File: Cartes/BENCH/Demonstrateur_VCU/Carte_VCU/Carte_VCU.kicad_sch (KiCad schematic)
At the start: 46 parts, among them J1 Conn_01x02_Female, J10 Conn_01x02_Female, J11 Conn_01x02_Female, J12 Conn_01x04_Female, J13 Conn_01x03_Female, J14 Conn_01x03_Female, J15 Conn_01x03_Female, J2 Conn_01x02_Female, J3 Conn_01x02_Female, J4 Conn_01x02_Female, J5 Conn_01x02_Female, J6 Conn_01x02_Female, J7 Conn_01x02_Female, J8 Conn_01x03_Female, J9 Conn_01x03_Female, SW1 SW_Push_SPDT, SW2 SW_Push_SPDT, SW3 SW_Push_SPDT, SW4 SW_Push_SPDT, SW5 SW_MEC_5G, SW6 SW_Push_SPDT, SW7 SW_Push_SPDT, SW8 SW_Push_SPDT, SW9 SW_Push_SPDT

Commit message: Ajout du dongle SCS
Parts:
- D1, D10, D11, D2, D3, D4, D5, D6, D7, D8, D9: footprint LED_THT:LED_D5.0mm -> (none)
- J1, J10, J11, J2, J3, J4, J5, J6, J7: footprint Connector_JST:JST_EH_S2B-EH_1x02_P2.50mm_Horizontal -> (none)
- J12: footprint Connector_JST:JST_EH_S4B-EH_1x04_P2.50mm_Horizontal -> (none)
- J13, J14, J15: footprint Connector_JST:JST_EH_S3B-EH_1x03_P2.50mm_Horizontal -> (none)
- J8, J9: footprint Connector_JST:JST_EH_S3B-EH_1x03_P2.50mm_Horizontal -> Connector_Wuerth:Wuerth_WR-WTB_64800311622_1x03_P1.50mm_Vertical
- SW1, SW2, SW3, SW4, SW6, SW7, SW8, SW9: footprint Connector_JST:JST_EH_B3B-EH-A_1x03_P2.50mm_Vertical -> (none)
- SW5: footprint Connector_JST:JST_EH_B2B-EH-A_1x02_P2.50mm_Vertical -> (none)

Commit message: ESF tentative
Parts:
- D1, D10, D11, D2, D3, D4, D5, D6, D7, D8, D9: footprint (none) -> LED_THT:LED_D5.0mm
- J1, J10, J11, J2, J3, J4, J5, J6, J7: footprint (none) -> Connector_JST:JST_EH_S2B-EH_1x02_P2.50mm_Horizontal
- J12: footprint (none) -> Connector_JST:JST_EH_S4B-EH_1x04_P2.50mm_Horizontal
- J13, J14, J15: footprint (none) -> Connector_JST:JST_EH_S3B-EH_1x03_P2.50mm_Horizontal
- SW1, SW2, SW3, SW4, SW6, SW7, SW8, SW9: footprint (none) -> Connector_JST:JST_EH_B3B-EH-A_1x03_P2.50mm_Vertical
- SW5: footprint (none) -> Connector_JST:JST_EH_B2B-EH-A_1x02_P2.50mm_Vertical
- renumbered R6 to R10, R7 to R11, R8 to R12, R9 to R13, R10 to R14, R11 to R15, R1 to R5, R2 to R6, R3 to R7, R4 to R8, R5 to R9

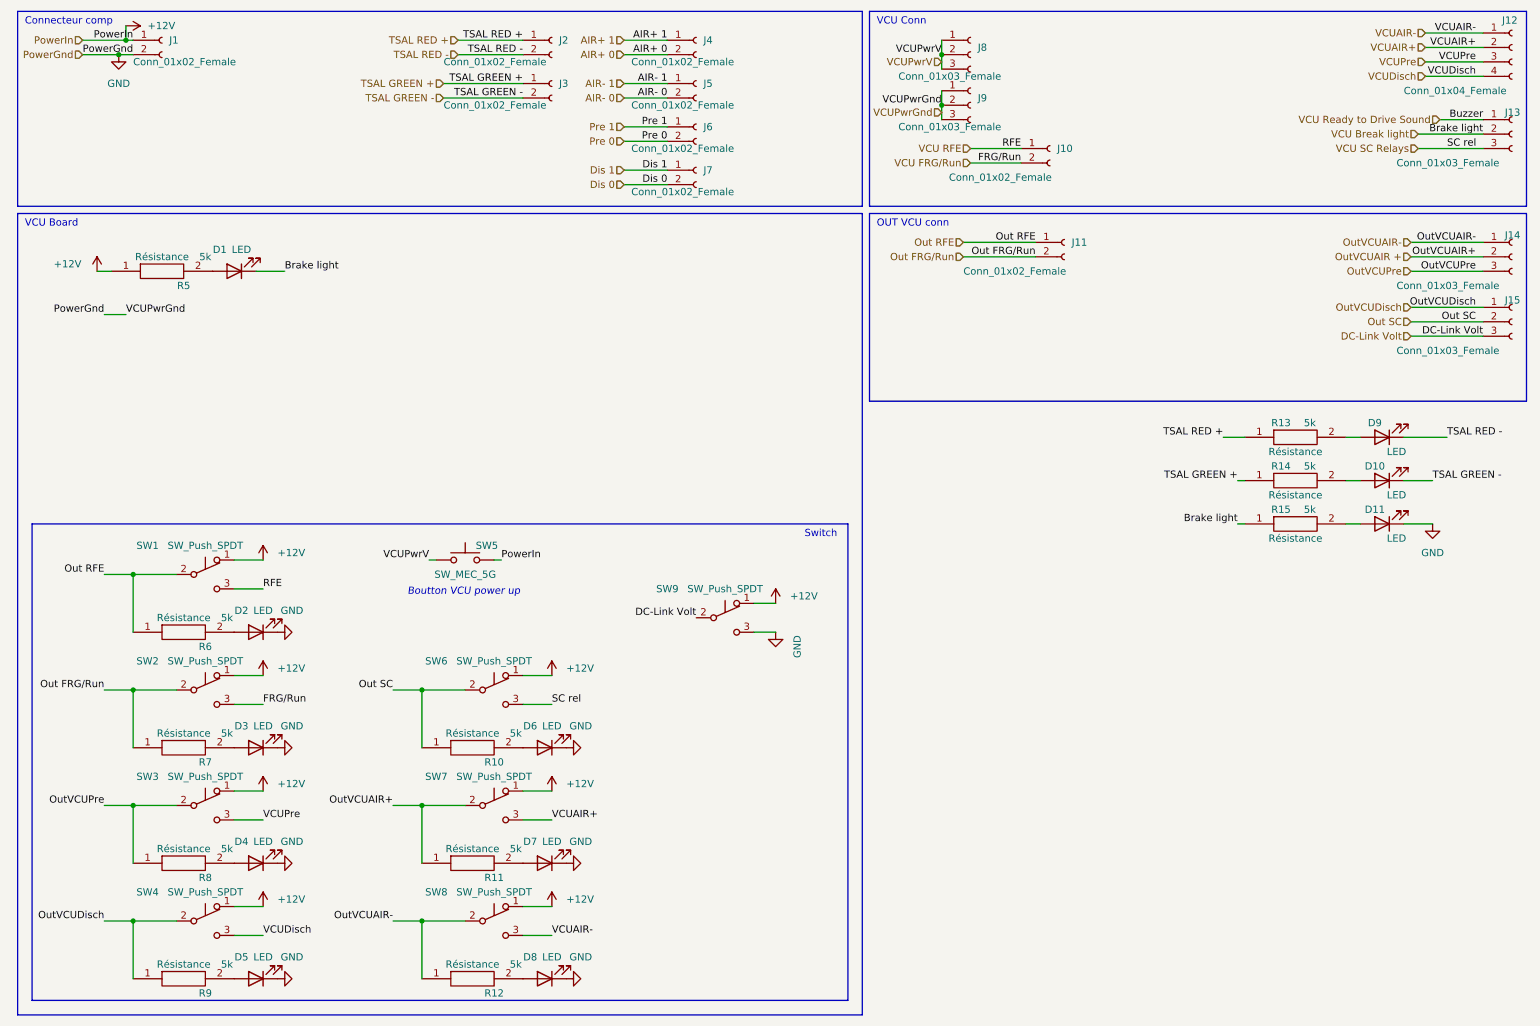
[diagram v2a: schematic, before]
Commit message: Ajout de l'AMS/IMD Reset
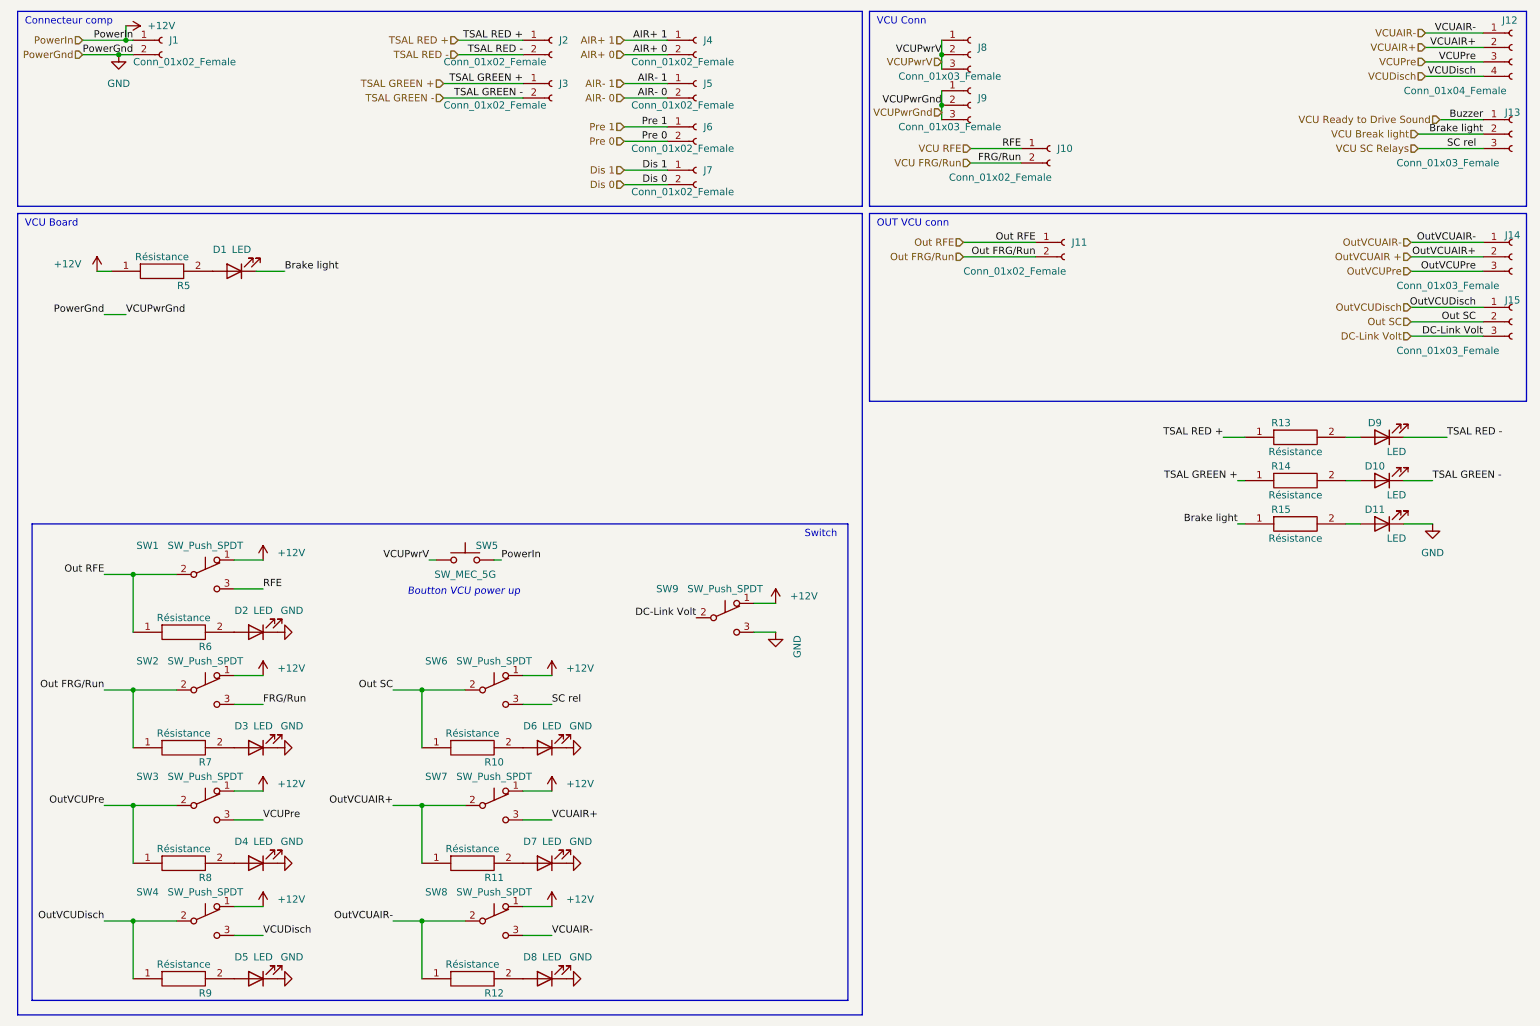
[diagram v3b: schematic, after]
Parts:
- R10, R11, R12, R13, R14, R15, R5, R6, R7, R8, R9: Spice_Model 5k -> (none); Spice_Netlist_Enabled Y -> (none); Spice_Primitive R -> (none)
